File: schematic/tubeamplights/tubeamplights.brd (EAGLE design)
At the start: 160 x 100 mm, 6 parts

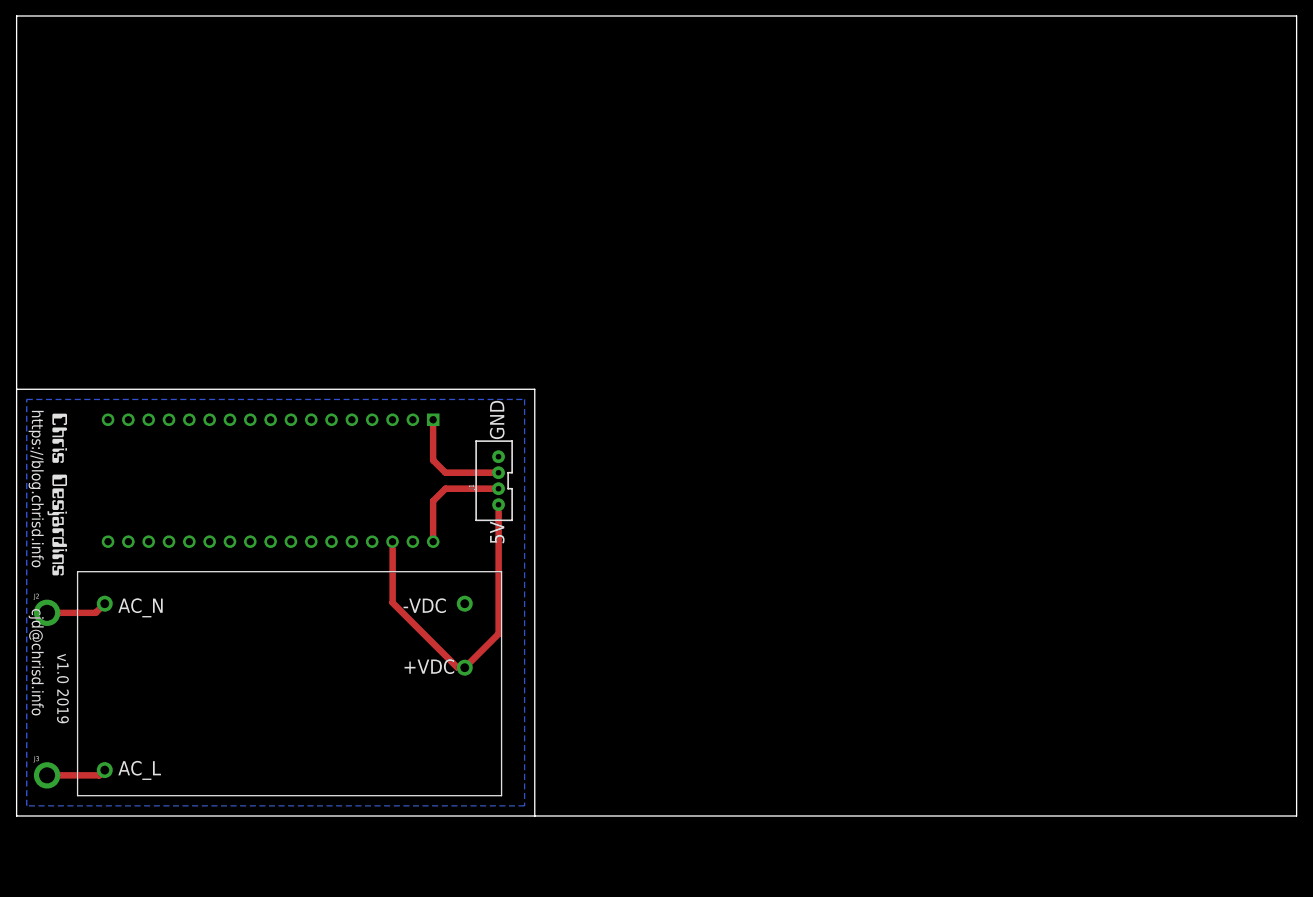
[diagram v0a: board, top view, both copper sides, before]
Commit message: Add mounting holes
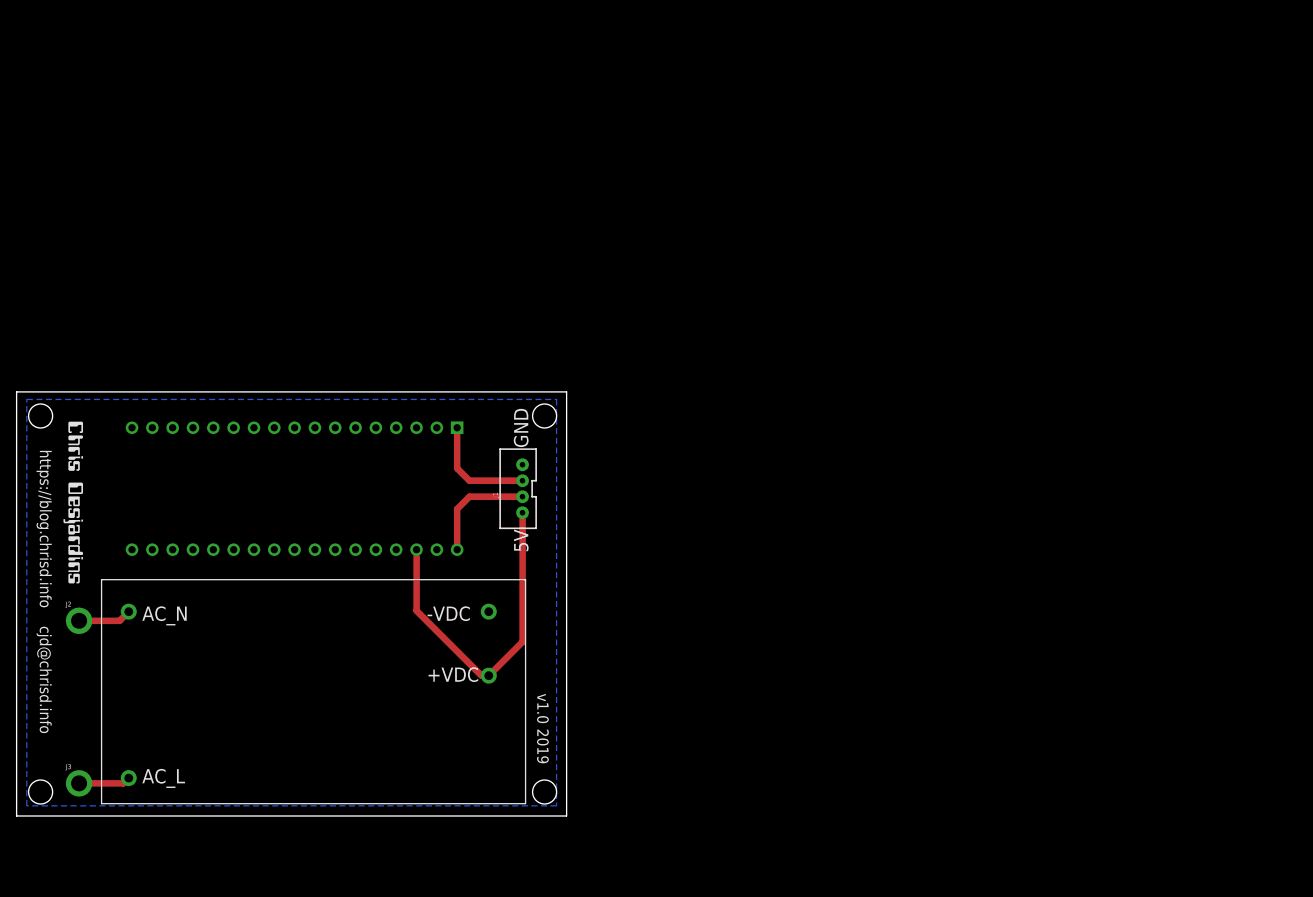
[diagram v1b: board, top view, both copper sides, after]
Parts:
- moved J2 4.12 mm to (7.81, 24.4)
- moved J3 4.12 mm to (7.81, 4.08)
- moved J1 3.16 mm to (62.7, 40.9)
- moved U$1 3.16 mm to (10.6, 49.8)
- moved U$2 3.16 mm to (10.6, 1.54)
- moved U$3 2.24 mm to (6.47, 49.4)
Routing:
- net AC_N: track 7.68 -> 6.68 mm
- net AC_L: track 7.48 -> 6.48 mm
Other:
- board size 160 x 100 mm -> 68.8 x 53 mm
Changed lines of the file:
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@@
 <setting verticaltext="up"/>
 </settings>
-<grid distance="50" unitdist="mil" unit="mil" style="lines" multiple="1" display="yes" altdistance="5" altunitdist="mil" altunit="mil"/>
+<grid distance="1" unitdist="mm" unit="mm" style="lines" multiple="1" display="yes" altdistance="1" altunitdist="mm" altunit="mm"/>
 <layers>
 <layer number="1" name="Top" color="4" fill="1" visible="yes" active="yes"/>
@@
 <layer number="43" name="vRestrict" color="2" fill="10" visible="yes" active="yes"/>
 <layer number="44" name="Drills" color="7" fill="1" visible="no" active="yes"/>
-<layer number="45" name="Holes" color="7" fill="1" visible="no" active="yes"/>
+<layer number="45" name="Holes" color="7" fill="1" visible="yes" active="yes"/>
 <layer number="46" name="Milling" color="3" fill="1" visible="no" active="yes"/>
 <layer number="47" name="Measures" color="7" fill="1" visible="no" active="yes"/>
@@
 <board>
 <plain>
-<wire x1="64.77" y1="0" x2="160" y2="0" width="0" layer="20"/>
-<wire x1="160" y1="0" x2="160" y2="100" width="0" layer="20"/>
-<wire x1="160" y1="100" x2="0" y2="100" width="0" layer="20"/>
-<wire x1="0" y1="100" x2="0" y2="53.34" width="0" layer="20"/>
-<wire x1="0" y1="0" x2="0" y2="53.34" width="0.1524" layer="20"/>
-<wire x1="0" y1="53.34" x2="64.77" y2="53.34" width="0.1524" layer="20"/>
-<wire x1="64.77" y1="53.34" x2="64.77" y2="0" width="0.1524" layer="20"/>
-<wire x1="64.77" y1="0" x2="0" y2="0" width="0.1524" layer="20"/>
-<text x="1.905" y="50.8" size="1.4224" layer="21" font="vector" rot="SR270">https://blog.chrisd.info         cjd@chrisd.info</text>
-<text x="60.96" y="36.83" size="1.778" layer="21" rot="R90" align="bottom-right">5V</text>
-<text x="60.96" y="46.99" size="1.778" layer="21" rot="R90">GND</text>
-<text x="5.08" y="20.32" size="1.4224" layer="21" font="vector" rot="SR270">v1.0 2019</text>
+<wire x1="0" y1="0" x2="68.75" y2="0" width="0" layer="20"/>
+<wire x1="68.75" y1="0" x2="68.75" y2="53.01" width="0" layer="20"/>
+<wire x1="68.75" y1="53.01" x2="0" y2="53.01" width="0" layer="20"/>
+<wire x1="0" y1="53.01" x2="0" y2="0" width="0" layer="20"/>
+<text x="2.905" y="45.8" size="1.4224" layer="21" font="vector" rot="SR270">https://blog.chrisd.info    cjd@chrisd.info</text>
+<text x="63.96" y="35.83" size="1.778" layer="21" rot="R90" align="bottom-right">5V</text>
+<text x="63.96" y="45.99" size="1.778" layer="21" rot="R90">GND</text>
+<text x="65.08" y="15.32" size="1.4224" layer="21" font="vector" rot="SR270">v1.0 2019</text>
+<hole x="66" y="3" drill="3"/>
+<hole x="66" y="50" drill="3"/>
+<hole x="3" y="50" drill="3"/>
+<hole x="3" y="3" drill="3"/>
 </plain>
 <attributes>
@@
 </autorouter>
 <elements>
-<element name="J1" library="SparkFun-Connectors" library_urn="urn:adsk.eagle:library:513" package="JST-4-PTH-VERT" package3d_urn="urn:adsk.eagle:package:38102/1" value="" x="59.69" y="41.91" smashed="yes" rot="R90">
-<attribute name="NAME" x="57.15" y="40.767" size="0.6096" layer="25" font="vector" ratio="20" rot="R90"/>
-<attribute name="PROD_ID" value="CONN-13251" x="140.97" y="59.69" size="1.778" layer="27" rot="R90" display="off"/>
-<attribute name="VALUE" x="62.992" y="40.259" size="0.6096" layer="27" font="vector" ratio="20" rot="R90"/>
+<element name="J1" library="SparkFun-Connectors" library_urn="urn:adsk.eagle:library:513" package="JST-4-PTH-VERT" package3d_urn="urn:adsk.eagle:package:38102/1" value="" x="62.69" y="40.91" smashed="yes" rot="R90">
+<attribute name="NAME" x="60.15" y="39.767" size="0.6096" layer="25" font="vector" ratio="20" rot="R90"/>
+<attribute name="PROD_ID" value="CONN-13251" x="143.97" y="58.69" size="1.778" layer="27" rot="R90" display="off"/>
+<attribute name="VALUE" x="65.992" y="39.259" size="0.6096" layer="27" font="vector" ratio="20" rot="R90"/>
 </element>
-<element name="J2" library="SparkFun-Connectors" library_urn="urn:adsk.eagle:library:513" package="1X01_2MM" package3d_urn="urn:adsk.eagle:package:38029/1" value="" x="3.81" y="25.4" smashed="yes">
-<attribute name="NAME" x="2.159" y="27.178" size="0.6096" layer="25" font="vector" ratio="20"/>
-<attribute name="VALUE" x="2.159" y="22.987" size="0.6096" layer="27" font="vector" ratio="20"/>
+<element name="J2" library="SparkFun-Connectors" library_urn="urn:adsk.eagle:library:513" package="1X01_2MM" package3d_urn="urn:adsk.eagle:package:38029/1" value="" x="7.81" y="24.4" smashed="yes">
+<attribute name="NAME" x="6.159" y="26.178" size="0.6096" layer="25" font="vector" ratio="20"/>
+<attribute name="VALUE" x="6.159" y="21.987" size="0.6096" layer="27" font="vector" ratio="20"/>
 </element>
-<element name="J3" library="SparkFun-Connectors" library_urn="urn:adsk.eagle:library:513" package="1X01_2MM" package3d_urn="urn:adsk.eagle:package:38029/1" value="" x="3.81" y="5.08" smashed="yes">
-<attribute name="NAME" x="2.159" y="6.858" size="0.6096" layer="25" font="vector" ratio="20"/>
-<attribute name="VALUE" x="2.159" y="2.667" size="0.6096" layer="27" font="vector" ratio="20"/>
+<element name="J3" library="SparkFun-Connectors" library_urn="urn:adsk.eagle:library:513" package="1X01_2MM" package3d_urn="urn:adsk.eagle:package:38029/1" value="" x="7.81" y="4.08" smashed="yes">
+<attribute name="NAME" x="6.159" y="5.858" size="0.6096" layer="25" font="vector" ratio="20"/>
+<attribute name="VALUE" x="6.159" y="1.667" size="0.6096" layer="27" font="vector" ratio="20"/>
 </element>
-<element name="U$1" library="ChrisD" package="ARDUINO_PRO_MICRO" value="ARDUINO_PRO_MICRO" x="7.62" y="50.8" smashed="yes" rot="R270"/>
-<element name="U$2" library="meanwell-mpm-20-x" package="MPM-20-X" value="MPM-20-X" x="7.62" y="2.54" smashed="yes"/>
-<element name="U$3" library="desjardins" package="LOGO" value="" x="4.4725" y="50.37" smashed="yes" rot="R270"/>
+<element name="U$1" library="ChrisD" package="ARDUINO_PRO_MICRO" value="ARDUINO_PRO_MICRO" x="10.62" y="49.8" smashed="yes" rot="R270"/>
+<element name="U$2" library="meanwell-mpm-20-x" package="MPM-20-X" value="MPM-20-X" x="10.62" y="1.54" smashed="yes"/>
+<element name="U$3" library="desjardins" package="LOGO" value="" x="6.4725" y="49.37" smashed="yes" rot="R270"/>
 </elements>
 <signals>
@@
 <contactref element="U$1" pad="P32"/>
 <contactref element="J1" pad="1"/>
-<wire x1="56.02" y1="18.54" x2="55.12" y2="18.54" width="0.8128" layer="1"/>
-<wire x1="55.12" y1="18.54" x2="46.99" y2="26.67" width="0.8128" layer="1"/>
-<wire x1="46.99" y1="26.67" x2="46.99" y2="34.29" width="0.8128" layer="1"/>
-<wire x1="60.24" y1="38.91" x2="60.24" y2="22.76" width="0.8128" layer="1"/>
-<wire x1="60.24" y1="22.76" x2="56.02" y2="18.54" width="0.8128" layer="1"/>
+<wire x1="59.02" y1="17.54" x2="58.12" y2="17.54" width="0.8128" layer="1"/>
+<wire x1="58.12" y1="17.54" x2="49.99" y2="25.67" width="0.8128" layer="1"/>
+<wire x1="49.99" y1="25.67" x2="49.99" y2="33.29" width="0.8128" layer="1"/>
+<wire x1="63.24" y1="37.91" x2="63.24" y2="21.76" width="0.8128" layer="1"/>
+<wire x1="63.24" y1="21.76" x2="59.02" y2="17.54" width="0.8128" layer="1"/>
 </signal>
 <signal name="GND">
@@
 <vertex x="1.27" y="1.27"/>
 <vertex x="1.27" y="52.07"/>
-<vertex x="63.5" y="52.07"/>
-<vertex x="63.5" y="1.27"/>
+<vertex x="67.5" y="52.07"/>
+<vertex x="67.5" y="1.27"/>
 </polygon>
 </signal>
@@
 <contactref element="U$2" pad="AC_N"/>
 <contactref element="J2" pad="1"/>
-<wire x1="11.02" y1="26.54" x2="9.88" y2="25.4" width="0.8128" layer="1"/>
-<wire x1="9.88" y1="25.4" x2="3.81" y2="25.4" width="0.8128" layer="1"/>
+<wire x1="14.02" y1="25.54" x2="12.88" y2="24.4" width="0.8128" layer="1"/>
+<wire x1="12.88" y1="24.4" x2="7.81" y2="24.4" width="0.8128" layer="1"/>
 </signal>
 <signal name="AC_L">
 <contactref element="U$2" pad="AC_L"/>
 <contactref element="J3" pad="1"/>
-<wire x1="11.02" y1="5.74" x2="10.36" y2="5.08" width="0.8128" layer="1"/>
-<wire x1="10.36" y1="5.08" x2="3.81" y2="5.08" width="0.8128" layer="1"/>
+<wire x1="14.02" y1="4.74" x2="13.36" y2="4.08" width="0.8128" layer="1"/>
+<wire x1="13.36" y1="4.08" x2="7.81" y2="4.08" width="0.8128" layer="1"/>
 </signal>
 <signal name="SCK">
 <contactref element="U$1" pad="P34"/>
 <contactref element="J1" pad="2"/>
-<wire x1="60.24" y1="40.91" x2="53.61" y2="40.91" width="0.8128" layer="1"/>
-<wire x1="53.61" y1="40.91" x2="52.07" y2="39.37" width="0.8128" layer="1"/>
-<wire x1="52.07" y1="39.37" x2="52.07" y2="34.29" width="0.8128" layer="1"/>
+<wire x1="63.24" y1="39.91" x2="56.61" y2="39.91" width="0.8128" layer="1"/>
+<wire x1="56.61" y1="39.91" x2="55.07" y2="38.37" width="0.8128" layer="1"/>
+<wire x1="55.07" y1="38.37" x2="55.07" y2="33.29" width="0.8128" layer="1"/>
 </signal>
 <signal name="MOSI">
 <contactref element="U$1" pad="P1"/>
 <contactref element="J1" pad="3"/>
-<wire x1="60.24" y1="42.91" x2="53.61" y2="42.91" width="0.8128" layer="1"/>
-<wire x1="53.61" y1="42.91" x2="52.07" y2="44.45" width="0.8128" layer="1"/>
-<wire x1="52.07" y1="44.45" x2="52.07" y2="49.53" width="0.8128" layer="1"/>
+<wire x1="63.24" y1="41.91" x2="56.61" y2="41.91" width="0.8128" layer="1"/>
+<wire x1="56.61" y1="41.91" x2="55.07" y2="43.45" width="0.8128" layer="1"/>
+<wire x1="55.07" y1="43.45" x2="55.07" y2="48.53" width="0.8128" layer="1"/>
 </signal>
 </signals>
